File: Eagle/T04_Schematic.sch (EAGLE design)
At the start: 29 parts

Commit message: Minor Tweaks and Fixes
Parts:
- renumbered PIN_MICRO_MAESTRO to MICRO_MAESTRO, PIN_MMA8452Q to MMA8452Q
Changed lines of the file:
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@@
 <part name="FRAME1" library="frames" deviceset="FRAME_A_L" device=""/>
 <part name="ATMEGA328" library="atmel" deviceset="MEGA8-P" device=""/>
-<part name="PIN_MMA8452Q" library="pinhead" deviceset="PINHD-1X6" device="" value="1x6"/>
-<part name="PIN_MICRO_MAESTRO" library="pinhead" deviceset="PINHD-1X5" device="" value="1x5"/>
+<part name="MMA8452Q" library="pinhead" deviceset="PINHD-1X6" device="" value="1x6"/>
+<part name="MICRO_MAESTRO" library="pinhead" deviceset="PINHD-1X5" device="" value="1x5"/>
 <part name="D24V5F3" library="pinhead" deviceset="PINHD-1X4" device="" value="1x4"/>
 <part name="TERMINAL_BATT_IN" library="pinhead" deviceset="PINHD-1X2" device="" value="1x2"/>
@@
 <instance part="FRAME1" gate="G$2" x="158.75" y="-50.8"/>
 <instance part="ATMEGA328" gate="G$1" x="121.92" y="88.9"/>
-<instance part="PIN_MMA8452Q" gate="A" x="181.61" y="137.16"/>
-<instance part="PIN_MICRO_MAESTRO" gate="A" x="222.25" y="106.68" smashed="yes">
+<instance part="MMA8452Q" gate="A" x="181.61" y="137.16"/>
+<instance part="MICRO_MAESTRO" gate="A" x="222.25" y="106.68" smashed="yes">
 <attribute name="NAME" x="210.82" y="114.935" size="1.778" layer="95"/>
 <attribute name="VALUE" x="215.9" y="96.52" size="1.778" layer="96"/>
@@
 </segment>
 <segment>
-<pinref part="PIN_MMA8452Q" gate="A" pin="6"/>
+<pinref part="MMA8452Q" gate="A" pin="6"/>
 <pinref part="GND3" gate="1" pin="GND"/>
 <wire x1="171.45" y1="130.81" x2="172.72" y2="132.08" width="0.1524" layer="91"/>
@@
 <pinref part="GND4" gate="1" pin="GND"/>
 <wire x1="205.74" y1="115.57" x2="208.28" y2="115.57" width="0.1524" layer="91"/>
-<pinref part="PIN_MICRO_MAESTRO" gate="A" pin="1"/>
+<pinref part="MICRO_MAESTRO" gate="A" pin="1"/>
 <wire x1="208.28" y1="115.57" x2="212.09" y2="111.76" width="0.1524" layer="91"/>
 <wire x1="212.09" y1="111.76" x2="219.71" y2="111.76" width="0.1524" layer="91"/>
@@
 <net name="SDA" class="0">
 <segment>
-<pinref part="PIN_MMA8452Q" gate="A" pin="2"/>
+<pinref part="MMA8452Q" gate="A" pin="2"/>
 <wire x1="179.07" y1="142.24" x2="160.02" y2="142.24" width="0.1524" layer="91"/>
 <label x="160.02" y="142.24" size="1.778" layer="95"/>
@@
 <net name="SCL" class="0">
 <segment>
-<pinref part="PIN_MMA8452Q" gate="A" pin="3"/>
+<pinref part="MMA8452Q" gate="A" pin="3"/>
 <wire x1="179.07" y1="139.7" x2="162.56" y2="139.7" width="0.1524" layer="91"/>
 <label x="162.56" y="139.7" size="1.778" layer="95"/>
@@
 <net name="INT0" class="0">
 <segment>
-<pinref part="PIN_MMA8452Q" gate="A" pin="4"/>
+<pinref part="MMA8452Q" gate="A" pin="4"/>
 <wire x1="179.07" y1="137.16" x2="165.1" y2="137.16" width="0.1524" layer="91"/>
 <label x="165.1" y="137.16" size="1.778" layer="95"/>
@@
 <pinref part="ATMEGA328" gate="G$1" pin="PD3(INT1)"/>
 <wire x1="162.56" y1="86.36" x2="147.32" y2="86.36" width="0.1524" layer="91"/>
-<pinref part="PIN_MMA8452Q" gate="A" pin="5"/>
+<pinref part="MMA8452Q" gate="A" pin="5"/>
 <wire x1="179.07" y1="134.62" x2="167.64" y2="134.62" width="0.1524" layer="91"/>
 <label x="167.64" y="134.62" size="1.778" layer="95"/>
@@
 </segment>
 <segment>
-<pinref part="PIN_MMA8452Q" gate="A" pin="1"/>
+<pinref part="MMA8452Q" gate="A" pin="1"/>
 <wire x1="172.72" y1="144.78" x2="179.07" y2="144.78" width="0.1524" layer="91"/>
 <pinref part="P+5" gate="VCC" pin="VCC"/>
@@
 <net name="RXD" class="0">
 <segment>
-<pinref part="PIN_MICRO_MAESTRO" gate="A" pin="3"/>
+<pinref part="MICRO_MAESTRO" gate="A" pin="3"/>
 <wire x1="187.96" y1="106.68" x2="219.71" y2="106.68" width="0.1524" layer="91"/>
 <label x="208.28" y="106.68" size="1.778" layer="95"/>
@@
 <net name="SERVO_TXD" class="0">
 <segment>
-<pinref part="PIN_MICRO_MAESTRO" gate="A" pin="4"/>
+<pinref part="MICRO_MAESTRO" gate="A" pin="4"/>
 <wire x1="185.42" y1="104.14" x2="219.71" y2="104.14" width="0.1524" layer="91"/>
 <pinref part="ATMEGA328" gate="G$1" pin="PD0(RXD)"/>
@@
 </segment>
 <segment>
-<pinref part="PIN_MICRO_MAESTRO" gate="A" pin="2"/>
+<pinref part="MICRO_MAESTRO" gate="A" pin="2"/>
 <wire x1="219.71" y1="109.22" x2="200.66" y2="109.22" width="0.1524" layer="91"/>
 <wire x1="200.66" y1="109.22" x2="199.39" y2="110.49" width="0.1524" layer="91"/>

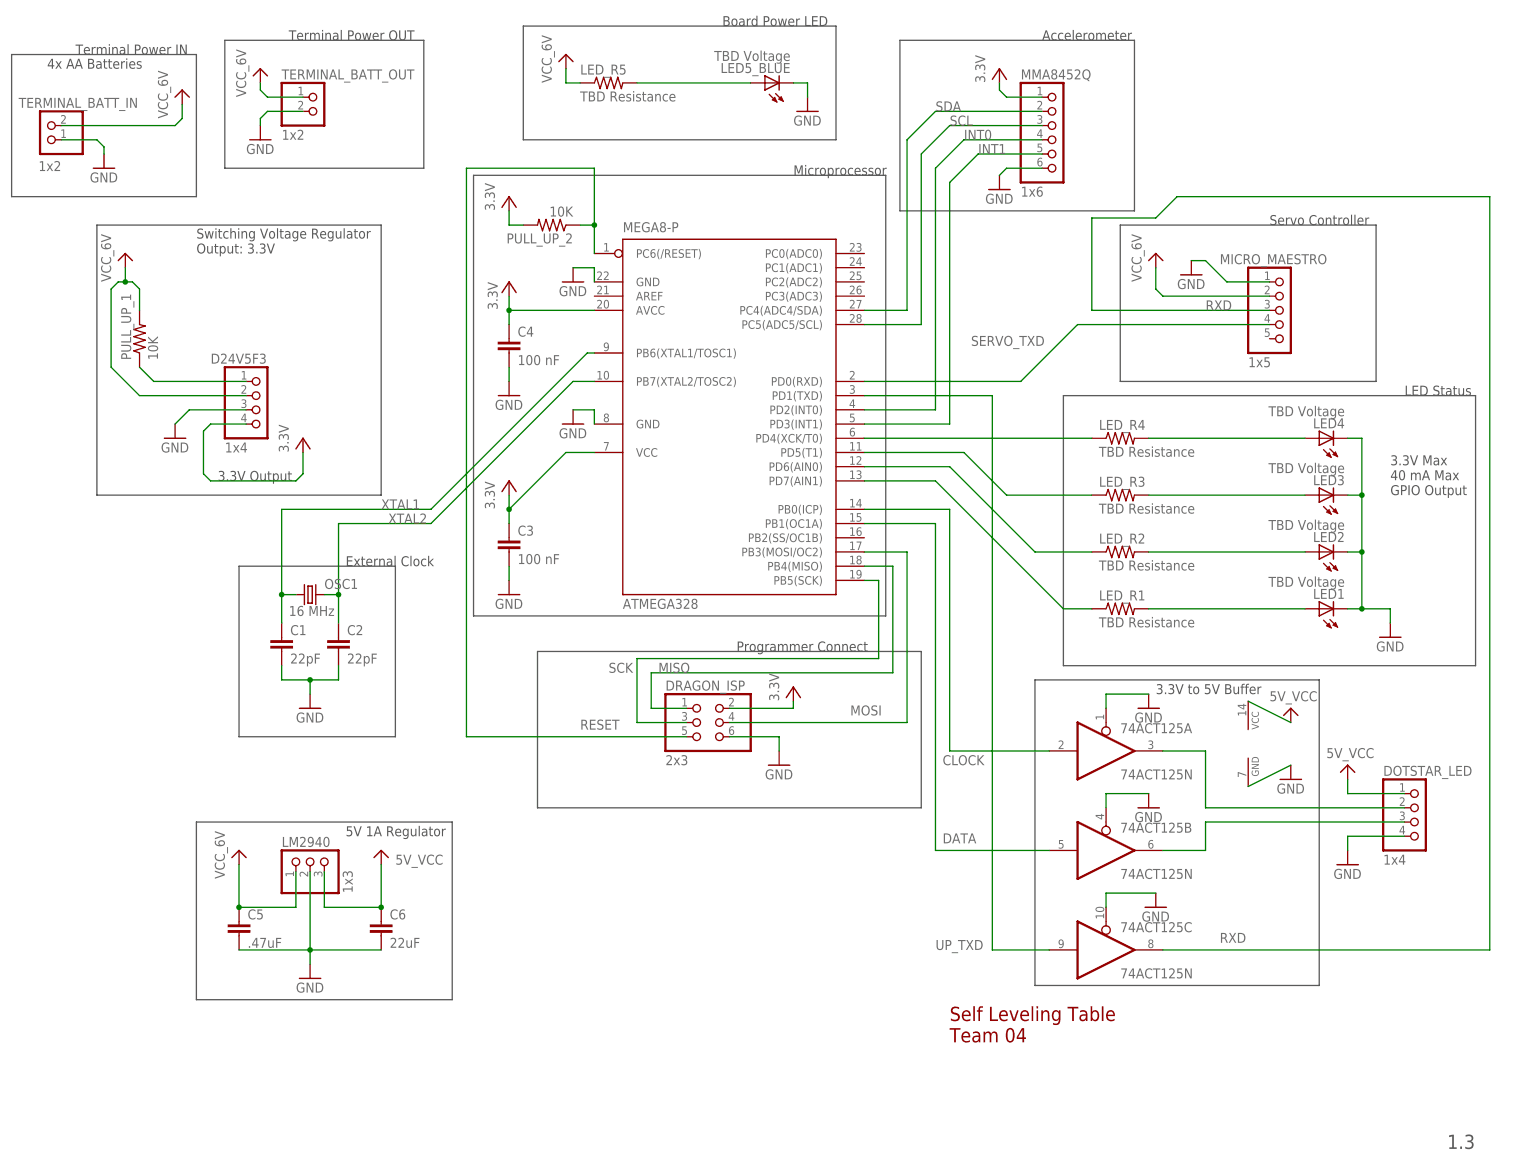
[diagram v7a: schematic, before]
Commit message: Added Andrew's Changes and Some more Silk Screen ID
Hi Taylor,

> We've been getting great feedback from you on our schematic/layout and
I
> was wondering if you could take one last look at our layout to see if
we
> missed anything major before we submit it.

I didn't have much time to look, but here you go:

Schematic:

- IMPORTANT: Chip "74ACT125" has an uninvoked gate. It's a quad buffer
part, and one of the buffers isn't hooked up. Use the INVOKE command in
eagle and click on that part to get the fourth buffer. Tie the input and
the enable line to low/high as you see fit -- but don't leave it
floating, like it is now.

- IMPORTANT: Chip "74ACT125" needs aq bypass cap.

- NOT IMPORTANT: Usually schematics have part identifiers that have
non-semantic meanings: like R1, R2, R3 not "PULL_UP_1". This is because
things move around a lot, and it's easier to type, and not get mixed up.
That said, I don't really care, feel free to leave it that way. But in
general, with schematics you share with others, I'd stick with regular
part identifiers.

Layout:

- MAYBE IMPORTANT: your ISP connector is a little close to the chip
below it and conector above. I think you'll be OK, but I'm not sure -
you might want to move that other connector a bit up away from the ISP
connector. But if you've printed it out and it looks OK, ignore this.

- NOT IMPORTANT: your board mounting holes are 0.115 inches, which is a
REALLY tight fit for a #4 screw. You might want to open it up to 0.125
if you have room.

- Otherwise: Looks great!
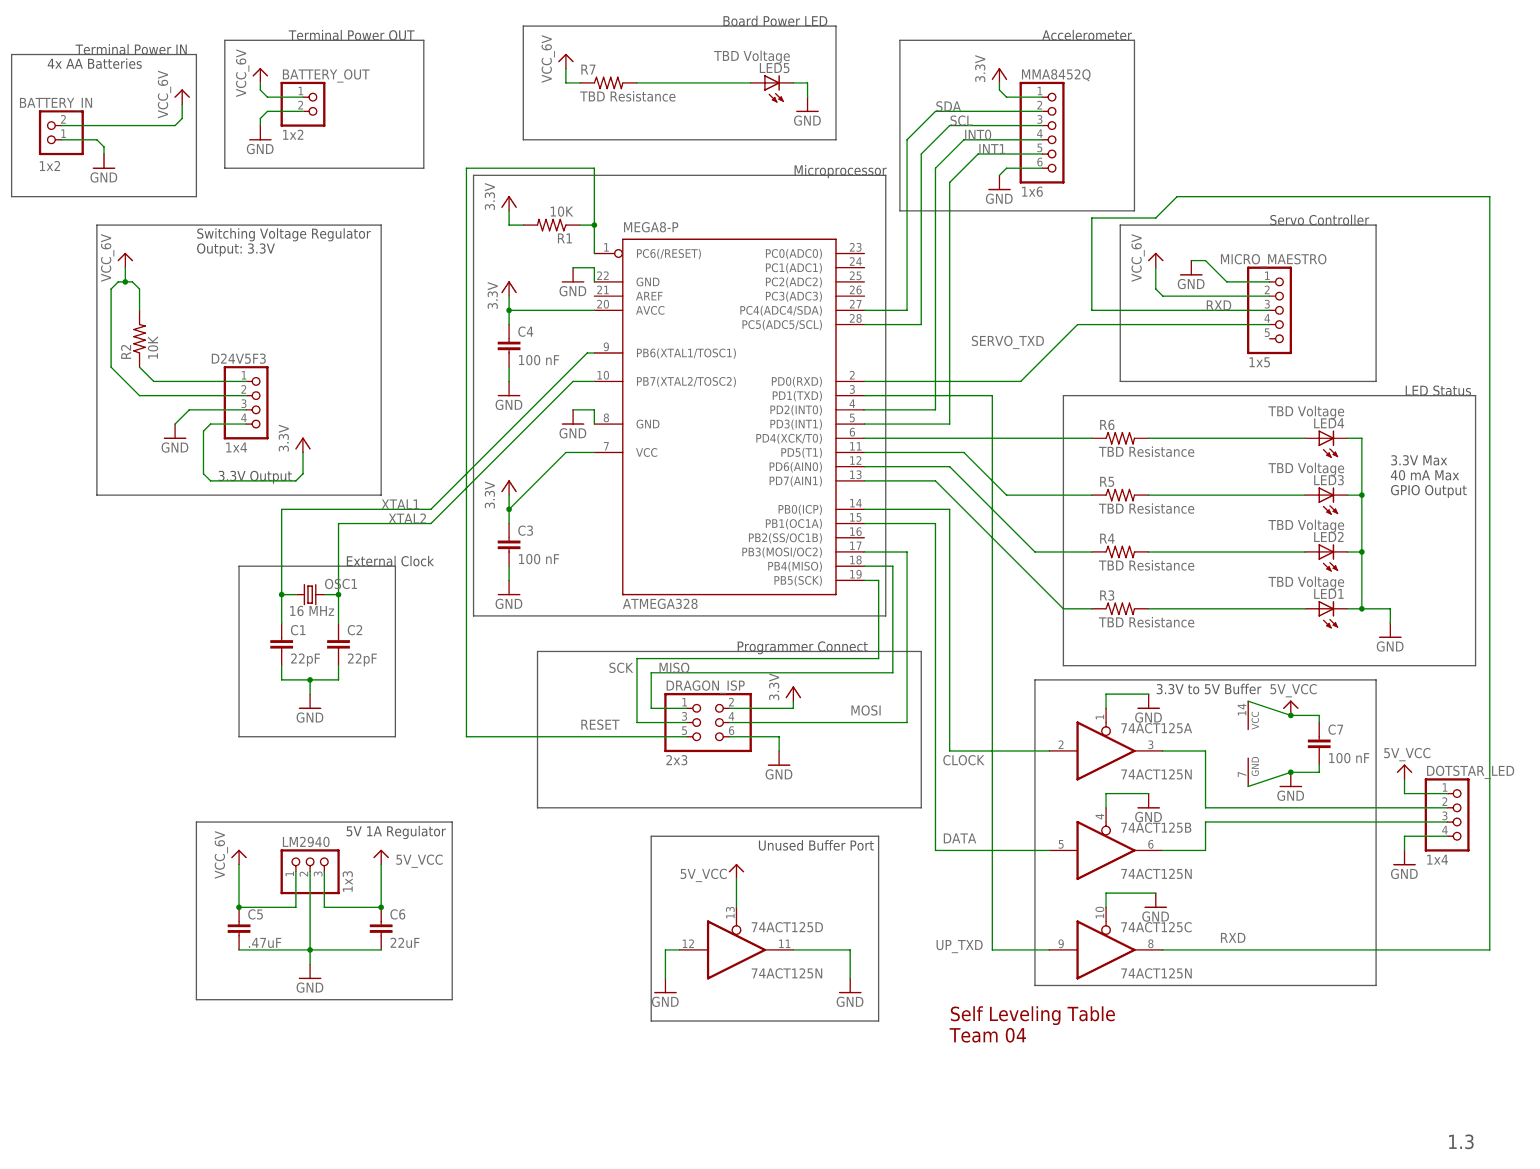
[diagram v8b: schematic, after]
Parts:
- added C7: 100 nF, rcl:C-EUC1206
- renumbered LED5_BLUE to LED5, LED_R1 to R3, LED_R2 to R4, LED_R3 to R5, LED_R4 to R6, LED_R5 to R7, PULL_UP_1 to R2, PULL_UP_2 to R1, TERMINAL_BATT_IN to BATTERY_IN, TERMINAL_BATT_OUT to BATTERY_OUT
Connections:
- net 5V_VCC: now also 74ACT125D.OE, C7.1
- net GND: now also 74ACT125D.I, 74ACT125D.O, C7.2
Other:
- note added: "Unused Buffer Port"
- moved on the sheet: DOTSTAR_LED
